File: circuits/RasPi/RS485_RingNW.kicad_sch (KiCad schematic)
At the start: 30 parts, among them J13 Conn_01x06_MountingPin, J8 Conn_01x06_MountingPin, Q17 S8550, Q5 S8550, U11 MAX3485, U12 MAX3485, U14 MAX3485, U16 MAX3485

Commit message: 無線&UI完成？
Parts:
- added JP1, JP2, JP3, JP4: Jumper_2_Open, Connector_PinHeader_2.54mm:PinHeader_1x02_P2.54mm_Vertical, symbol Jumper:Jumper_2_Open
- renumbered C21 to C11, C22 to C12, C35 to C13, C36 to C14, J8 to J2, J13 to J3, Q5 to Q1, Q17 to Q2, R71 to R11, R78 to R12, R77 to R13, R87 to R14, R88 to R15, R79 to R16, R80 to R17, R90 to R18, R89 to R19, R71 to R20, R72 to R21, R73 to R22, R74 to R23, R75 to R24, R76 to R25, R77 to R26, R78 to R27, R79 to R28, U16 to U2, U14 to U3, U11 to U4, U12 to U5
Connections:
- net MainRX_RS485RingX_TX renamed MainRX_RS485X_TX
- net MainRX_RS485RingY_TX renamed MainRX_RS485Y_TX
- net MainTX_RS485RingX_RX renamed MainTX_RS485X_RX
- net MainTX_RS485RingY_RX renamed MainTX_RS485Y_RX
- net RS485RingX_RA renamed RS485X_RA
- net RS485X_RA: now also JP2.1 (A); no longer R19.1
- net RS485RingX_RB renamed RS485X_RB
- net RS485RingX_TA renamed RS485X_TA
- net RS485X_TA: now also JP1.1 (A); no longer R18.1
- net RS485RingX_TB renamed RS485X_TB
- net RS485RingY_RA renamed RS485Y_RA
- net RS485Y_RA: now also JP4.1 (A); no longer R28.1
- net RS485RingY_RB renamed RS485Y_RB
- net RS485RingY_TA renamed RS485Y_TA
- net RS485Y_TA: now also JP3.1 (A); no longer R27.1
- net RS485RingY_TB renamed RS485Y_TB
- new net: JP3.2 (B), R27.1
- new net: JP1.2 (B), R18.1
- new net: JP2.2 (B), R19.1
- new net: JP4.2 (B), R28.1
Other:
- moved on the sheet: R18, R19, R27, R28

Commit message: ラズパイ基板とか
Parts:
- removed C14: 0.1uF, Capacitor_SMD:C_0402_1005Metric, symbol Device:C
- removed JP1, JP2, JP3, JP4: Jumper_2_Open, Connector_PinHeader_2.54mm:PinHeader_1x02_P2.54mm_Vertical, symbol Jumper:Jumper_2_Open
- removed Q2: S8550, Package_TO_SOT_SMD:SOT-23, symbol Device:Q_PNP_BEC
- removed R24, R25, R26: 2.2k, Resistor_SMD:R_0402_1005Metric, symbol Device:R
- removed R27, R28: 120, Resistor_SMD:R_0402_1005Metric, symbol Device:R
- removed U5: MAX3485, Package_SO:SOP-8_3.9x4.9mm_P1.27mm, symbol Interface_UART:MAX3485
- added C38: 0.1uF, Capacitor_SMD:C_0402_1005Metric, symbol Device:C
- added Q22: S8550, Package_TO_SOT_SMD:SOT-23, symbol Device:Q_PNP_BEC
- added R90: 7.5k, Resistor_SMD:R_0603_1608Metric, symbol Device:R
- added R95: 20k, Resistor_SMD:R_0402_1005Metric, symbol Device:R
- added R96, R97: 2.2k, Resistor_SMD:R_0402_1005Metric, symbol Device:R
- added R98: 120, Resistor_SMD:R_0402_1005Metric, symbol Device:R
- added U14: MAX3485, Package_SO:SOP-8_3.9x4.9mm_P1.27mm, symbol Interface_UART:MAX3485
- R13, R22: value 10k -> 2.2k
- R15, R23: value 2.2k -> 120
- R16: value 2.2k -> 10k
- R18: value 120 -> 2.2k
- R20: value 7.5k -> 10k; footprint Resistor_SMD:R_0603_1608Metric -> Resistor_SMD:R_0402_1005Metric
- R21: value 20k -> 2.2k
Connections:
- net +3.3V: now also R13.1, R17.1, R21.1, C38.1, Q22.2 (E), R96.1, U14.8 (VCC); no longer R14.1, R16.1, R23.1
- net GNDD: now also R14.2, R16.2, R18.2, R20.2, C38.2, R95.2, R97.2, U14.5 (GND); no longer R13.2, R15.2, R17.2, R21.2
- net MainRX_RS485Y_TX: now also U4.1 (RO)
- net MainTX_RS485Y_RX: now also R90.2, U14.4 (DI); no longer R20.2, U4.4 (DI)
- net RS485X_RA: now also R17.2, R19.1; no longer R16.2
- net RS485X_RB: now also R18.1; no longer R17.1
- net RS485X_TA: now also R13.2, R15.1; no longer R14.2
- net RS485X_TB: now also R14.1, R15.2; no longer R15.1, R18.2
- net RS485Y_RA: now also R21.2, R23.1, U4.6 (A)
- net RS485Y_RB: now also R22.1, R23.2, U4.7 (B)
- net RS485Y_TA: now also R96.2, R98.1, U14.6 (A); no longer R23.2, U4.6 (A)
- net RS485Y_TB: now also R97.1, R98.2, U14.7 (B); no longer U4.7 (B)
- net at R20.1: now also U4.2 (~{RE}), U4.3 (DE)
- net at U3.2 (~{RE}), U3.3 (DE): now also R16.1; no longer R13.1
- new net: Q22.3 (C), R95.1, U14.2 (~{RE}), U14.3 (DE)
- new net: Q22.1 (B), R90.1

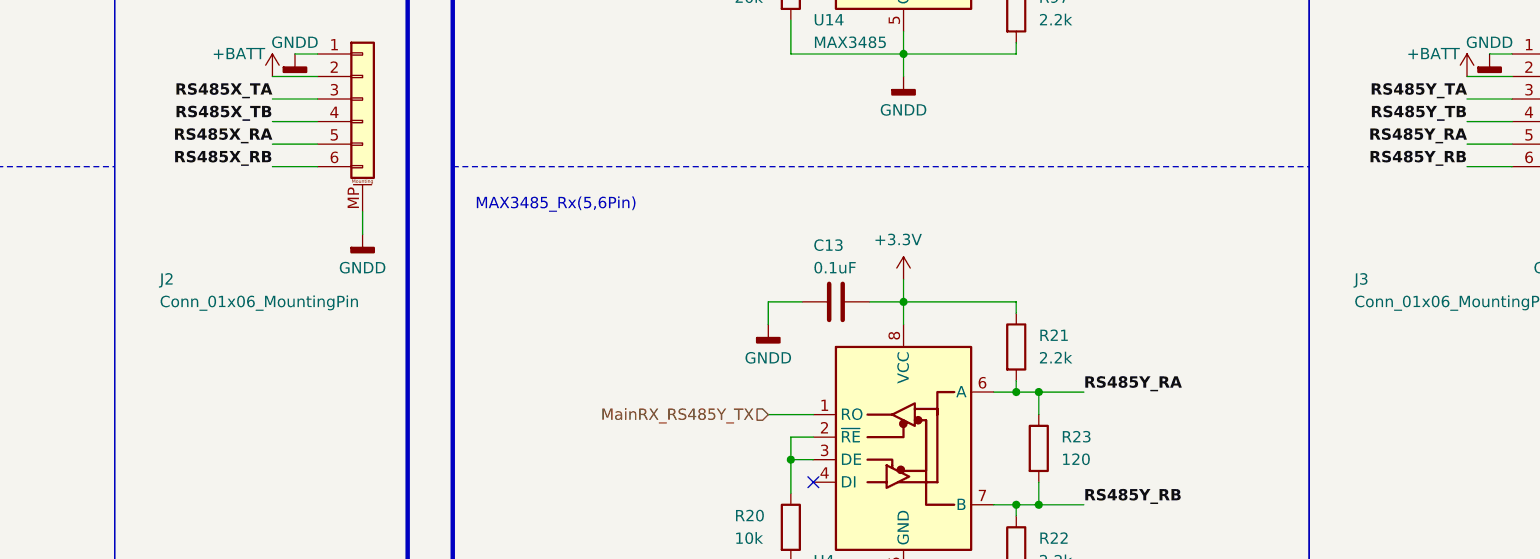
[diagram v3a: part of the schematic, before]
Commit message: 発注第2弾
RasPi発注
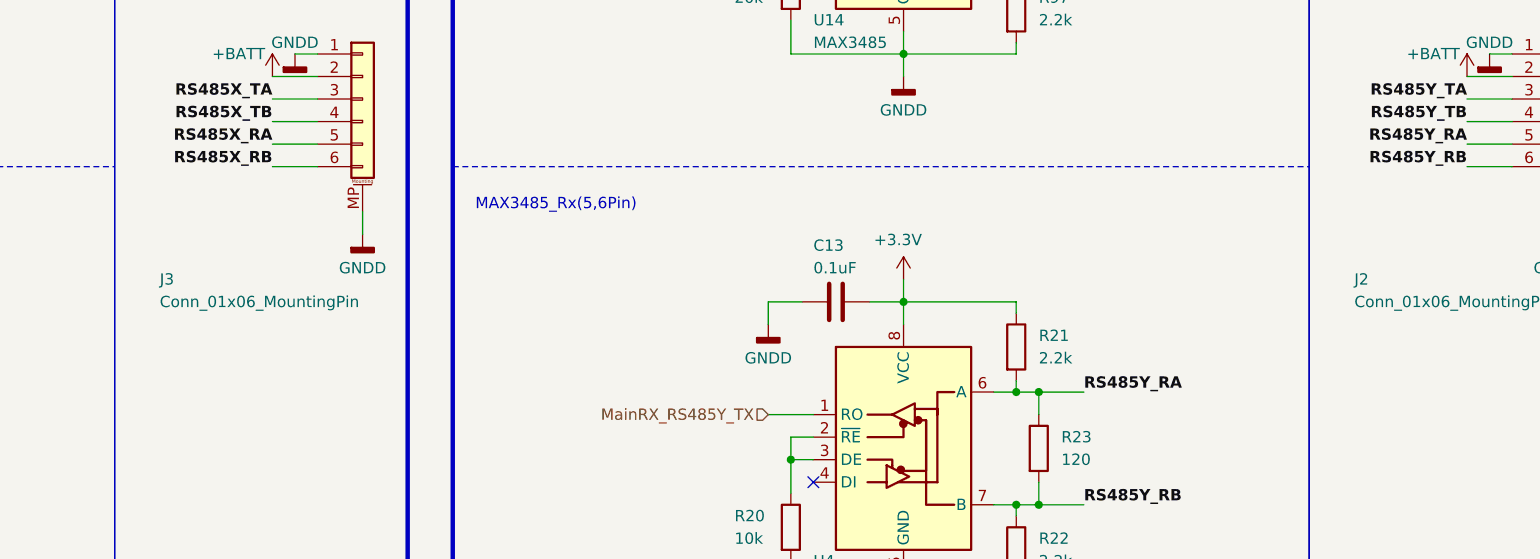
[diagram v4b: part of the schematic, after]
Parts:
- renumbered J3 to J2, J2 to J3
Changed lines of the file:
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@@
   (symbol (lib_id "Connector_Generic_MountingPin:Conn_01x06_MountingPin") (at 142.24 86.36 0) (unit 1)
     (in_bom yes) (on_board yes) (dnp no)
-    (property "Reference" "J2" (at 119.38 106.68 0)
+    (property "Reference" "J3" (at 119.38 106.68 0)
       (effects (font (size 1.27 1.27)) (justify left))
     )
@@
       (project "RasPi"
         (path "/689a9e74-f202-4ea4-bfbb-4341f2549250/24ae560a-4b26-4668-af95-4f511f2fb172/baf1d240-10ea-4c90-a2bd-711ba68a72a3"
-          (reference "J2") (unit 1)
+          (reference "J3") (unit 1)
         )
       )
@@
   (symbol (lib_id "Connector_Generic_MountingPin:Conn_01x06_MountingPin") (at 276.86 86.36 0) (unit 1)
     (in_bom yes) (on_board yes) (dnp no)
-    (property "Reference" "J3" (at 254 106.68 0)
+    (property "Reference" "J2" (at 254 106.68 0)
       (effects (font (size 1.27 1.27)) (justify left))
     )
@@
       (project "RasPi"
         (path "/689a9e74-f202-4ea4-bfbb-4341f2549250/24ae560a-4b26-4668-af95-4f511f2fb172/baf1d240-10ea-4c90-a2bd-711ba68a72a3"
-          (reference "J3") (unit 1)
-        )
-      )
+          (reference "J2") (unit 1)
+        )
+      )
